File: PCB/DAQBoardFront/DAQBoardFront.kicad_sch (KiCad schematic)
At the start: 20 parts, among them J1 STM32F103C_Blue_Pill, J2 53375-0410, U1 Accelerometer, U2 AdafruitCANPal

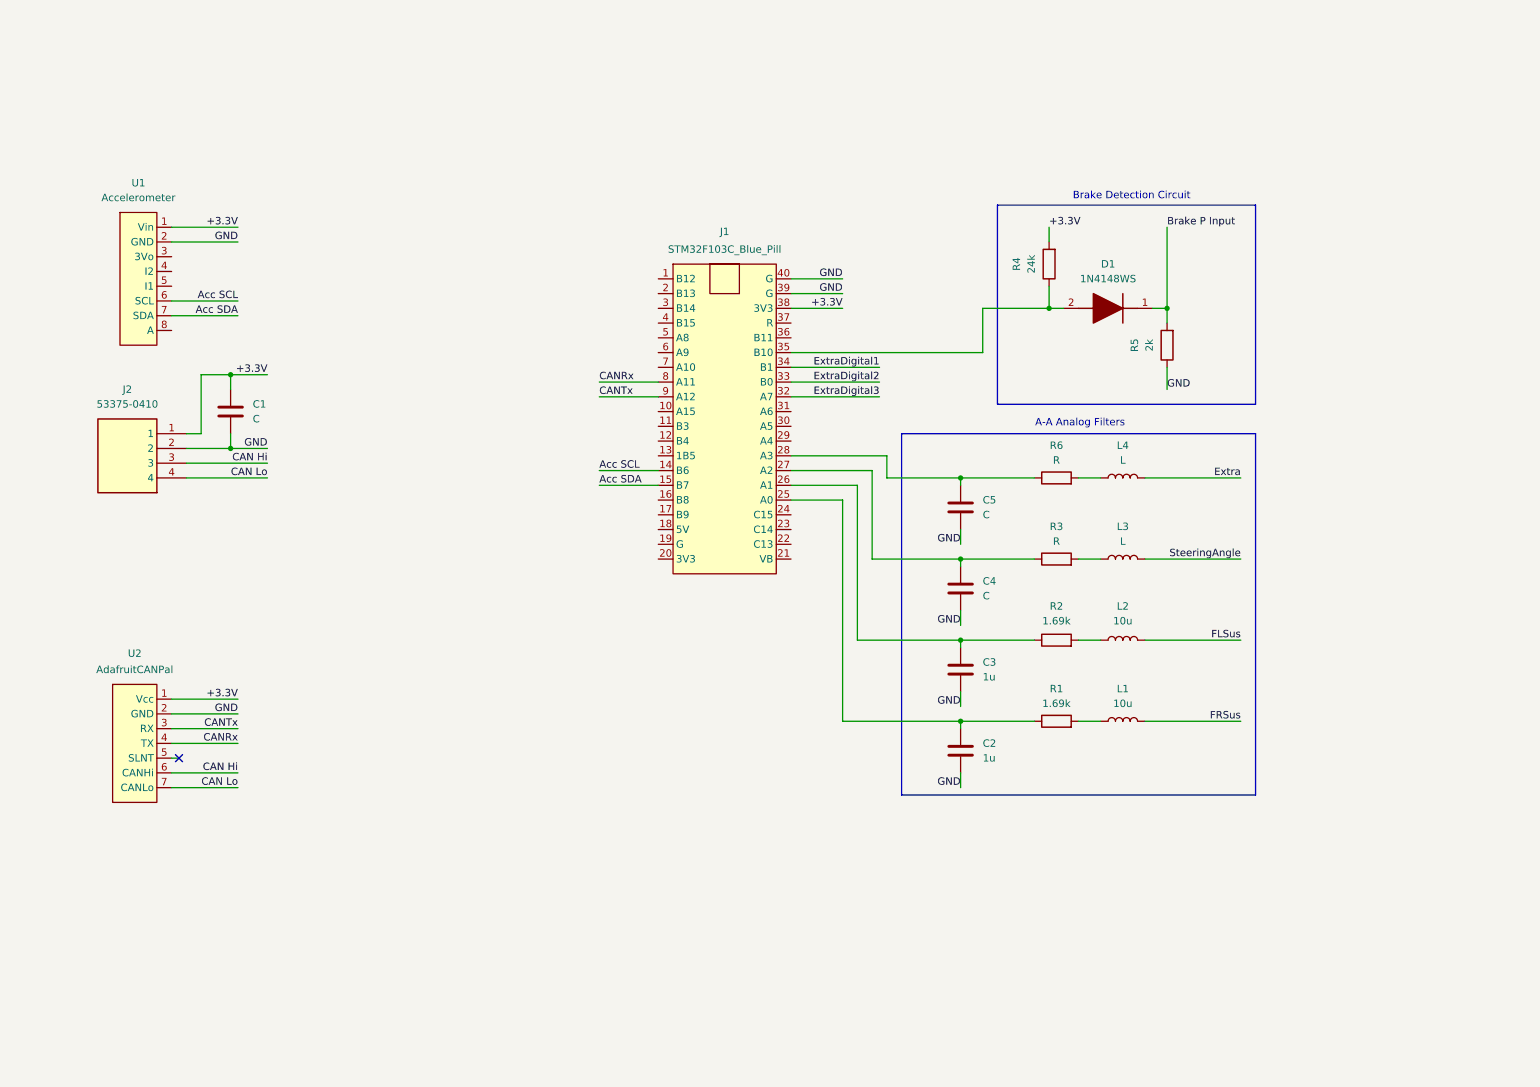
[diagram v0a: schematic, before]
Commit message: Initialized CFR symbol and footprint libraries, added git ignore file
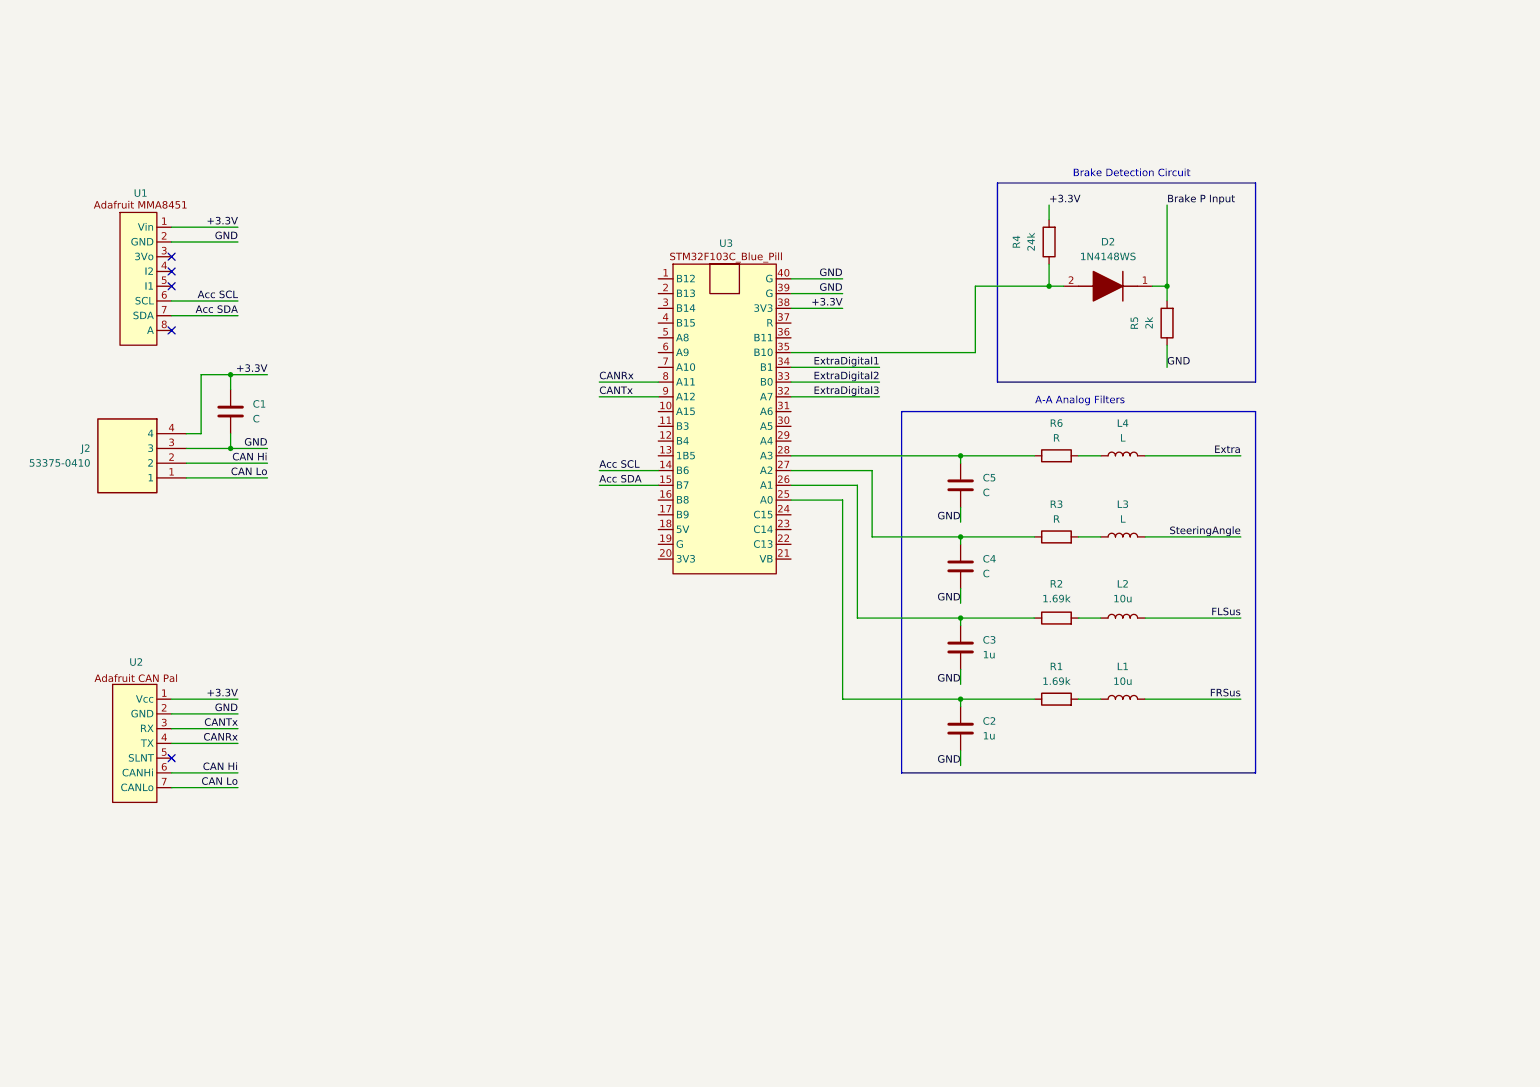
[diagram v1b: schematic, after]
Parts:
- removed D1: 1N4148WS, SODFL2512X90N, symbol 1N4148WS:1N4148WS
- removed J1: STM32F103C_Blue_Pill, symbol DAQ2027Lib:_Blue_Pill
- removed J2: 53375-0410, 0533750410, symbol 53375-0410:53375-0410
- removed U1: Accelerometer, symbol DAQ2027Lib:Adafruit_MMA8451
- removed U2: AdafruitCANPal, symbol DAQ2027Lib:Adafruit_CAN_Pal
- added D2: 1N4148WS, SODFL2512X90N, symbol CFR-Symbol-Library:1N4148WS
- added J2: 53375-0410, 0533750410, symbol CFR-Symbol-Library:53375-0410
- added U1: (no value), symbol CFR-Symbol-Library:Adafruit-MMA8451
- added U2: (no value), CFR-Footprint-Library:Adafruit CAN Pal, symbol CFR-Symbol-Library:Adafruit-CAN-Pal
- added U3: (no value), CFR-Footprint-Library:Blue-Pill, symbol CFR-Symbol-Library:Blue-Pill
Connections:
- net +3.3V: now also J2.4, U1.1 (Vin), U2.1 (Vcc), U3.38 (3V3)
- net Acc SCL: now also U1.6 (SCL), U3.14 (B6)
- net Acc SDA: now also U1.7 (SDA), U3.15 (B7)
- net Brake P Input: now also D2.1 (K)
- net CAN Hi: now also J2.2, U2.6 (CANHi)
- net CAN Lo: now also J2.1, U2.7 (CANLo)
- net CANRx: now also U2.4 (TX), U3.8 (A11)
- net CANTx: now also U2.3 (RX), U3.9 (A12)
- net ExtraDigital1: now also U3.34 (B1)
- net ExtraDigital2: now also U3.33 (B0)
- net ExtraDigital3: now also U3.32 (A7)
- net GND: now also J2.3, U1.2 (GND), U2.2 (GND), U3.39 (G), U3.40 (G)
- net at C2.1, R1.1: now also U3.25 (A0)
- net at C3.1, R2.1: now also U3.26 (A1)
- net at C4.1, R3.1: now also U3.27 (A2)
- net at C5.1, R6.1: now also U3.28 (A3)
- net at R4.1: now also D2.2 (A), U3.35 (B10)
- no-connect marks 1 -> 5
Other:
- moved on the sheet: C2, C3, C4, C5, L1, L2, L3, L4, R1, R2, R3, R4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

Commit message: Added more footprints/symbols for 8-pin input and SMD components
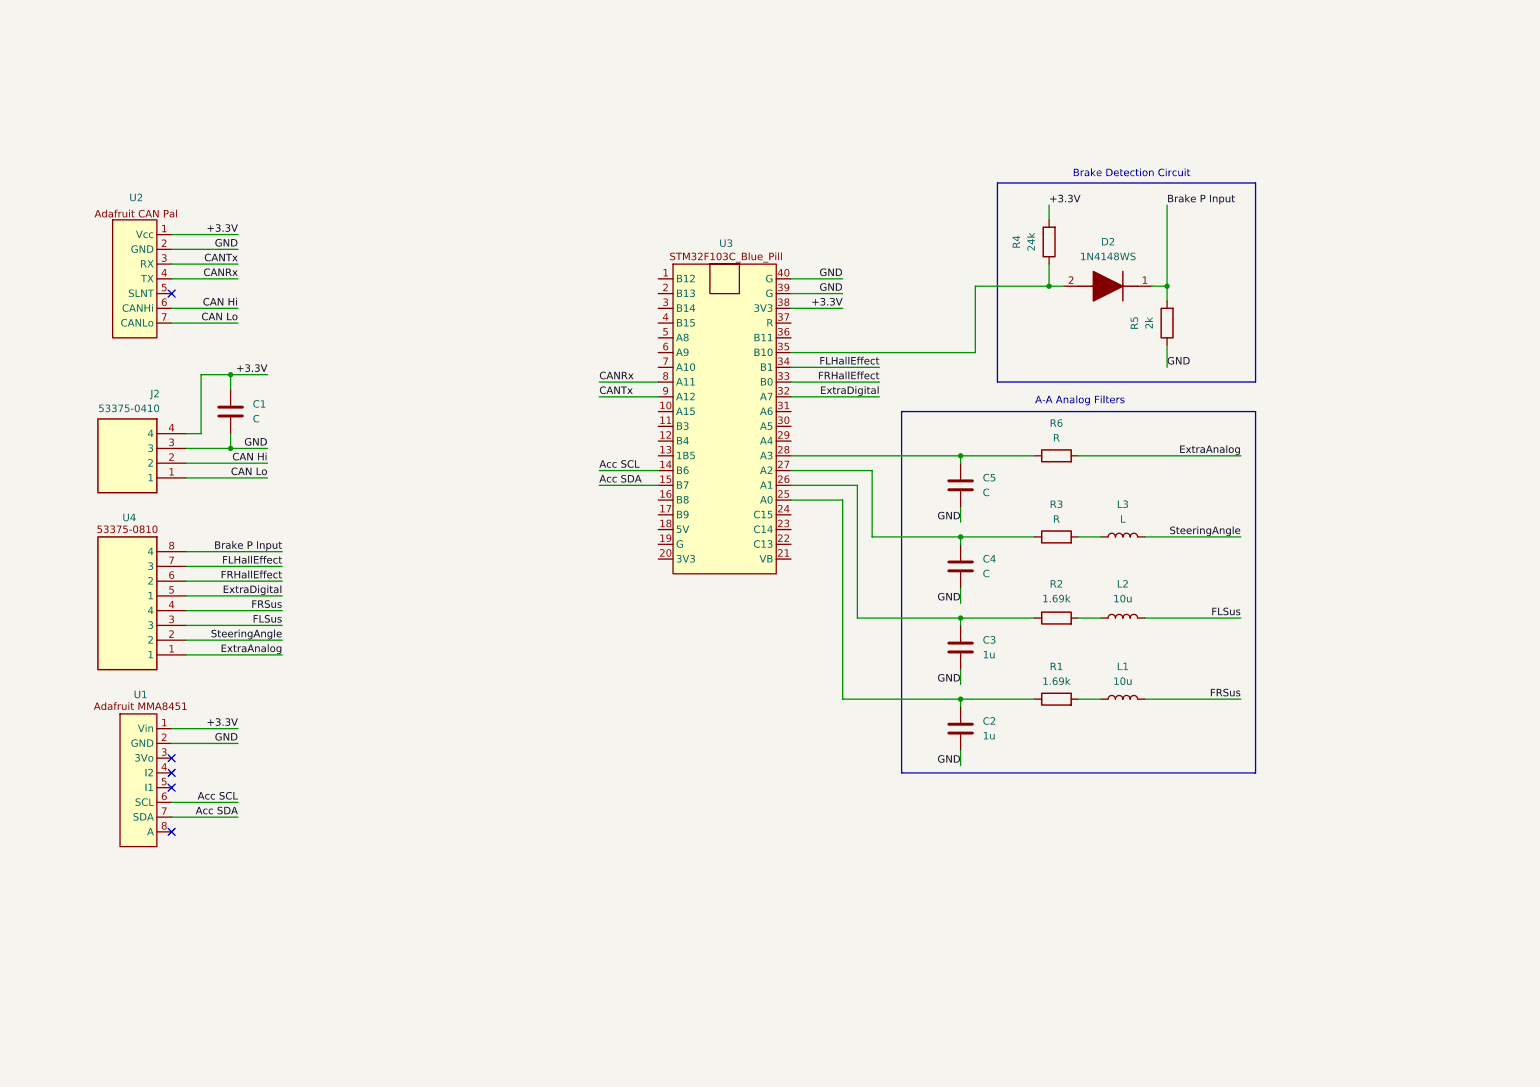
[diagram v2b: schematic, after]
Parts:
- removed L4: L, symbol Device:L
- added U4: (no value), CFR-Footprint-Library:CONN08_533750810_MOL, symbol CFR-Symbol-Library:53375-0810
- C1, C2, C3, C4, C5: footprint (none) -> Capacitor_SMD:C_0603_1608Metric_Pad1.08x0.95mm_HandSolder
- R1, R2, R3, R5, R6: footprint (none) -> Resistor_SMD:R_0603_1608Metric_Pad0.98x0.95mm_HandSolder
- R4: footprint (none) -> LED_SMD:LED_0603_1608Metric_Pad1.05x0.95mm_HandSolder
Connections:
- net Brake P Input: now also U4.8 (4)
- net FLSus: now also U4.3
- net FRSus: now also U4.4
- net SteeringAngle: now also U4.2
- net ExtraAnalog: now reaches R6.2
- net ExtraAnalog: now also U4.1
- net ExtraDigital1 renamed FLHallEffect
- net FLHallEffect: now also U4.7 (3)
- net ExtraDigital2 renamed FRHallEffect
- net FRHallEffect: now also U4.6 (2)
- net ExtraDigital3 renamed ExtraDigital
- net ExtraDigital: now also U4.5 (1)
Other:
- moved on the sheet: U1, U2

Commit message: Version 1.0 completed
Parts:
- L1, L2, L3: footprint (none) -> Inductor_SMD:L_0805_2012Metric_Pad1.05x1.20mm_HandSolder
- U1: footprint (none) -> CFR-Footprint-Library:MODULE_2019
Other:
- moved on the sheet: C1, C2, C3, C4, C5, D2, J2, L1, L2, L3, R1, R2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

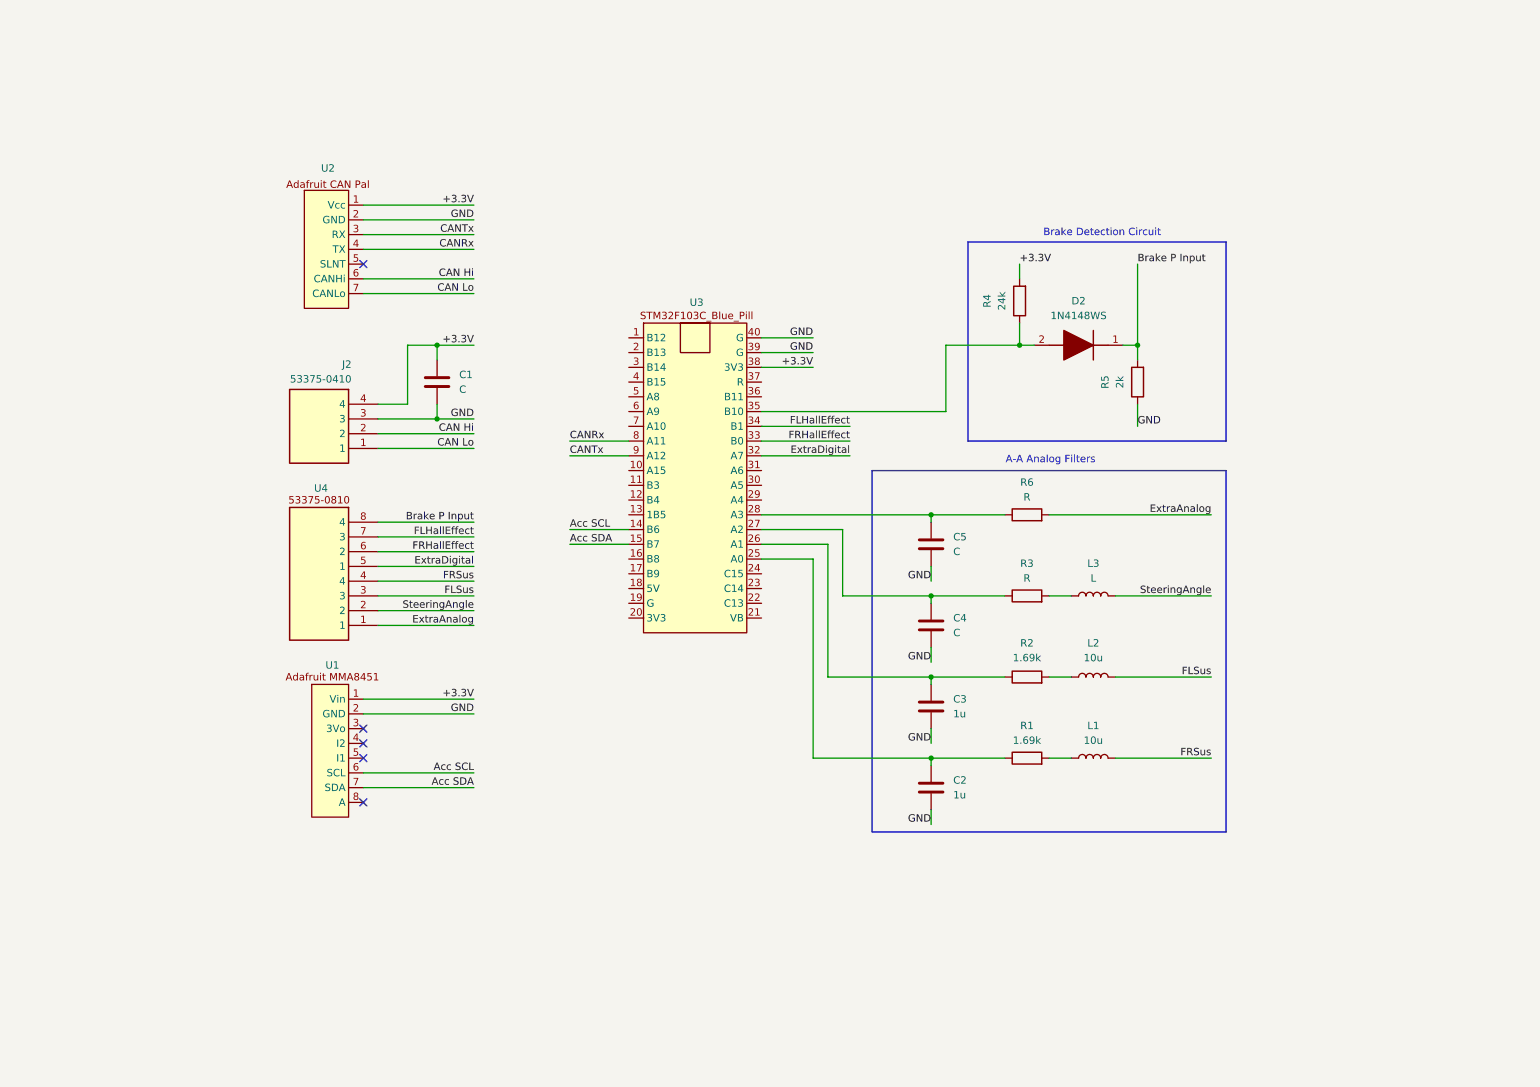
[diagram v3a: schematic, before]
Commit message: DAQ board moving towards multi-voltage level architecture & custom CAN module, WIP
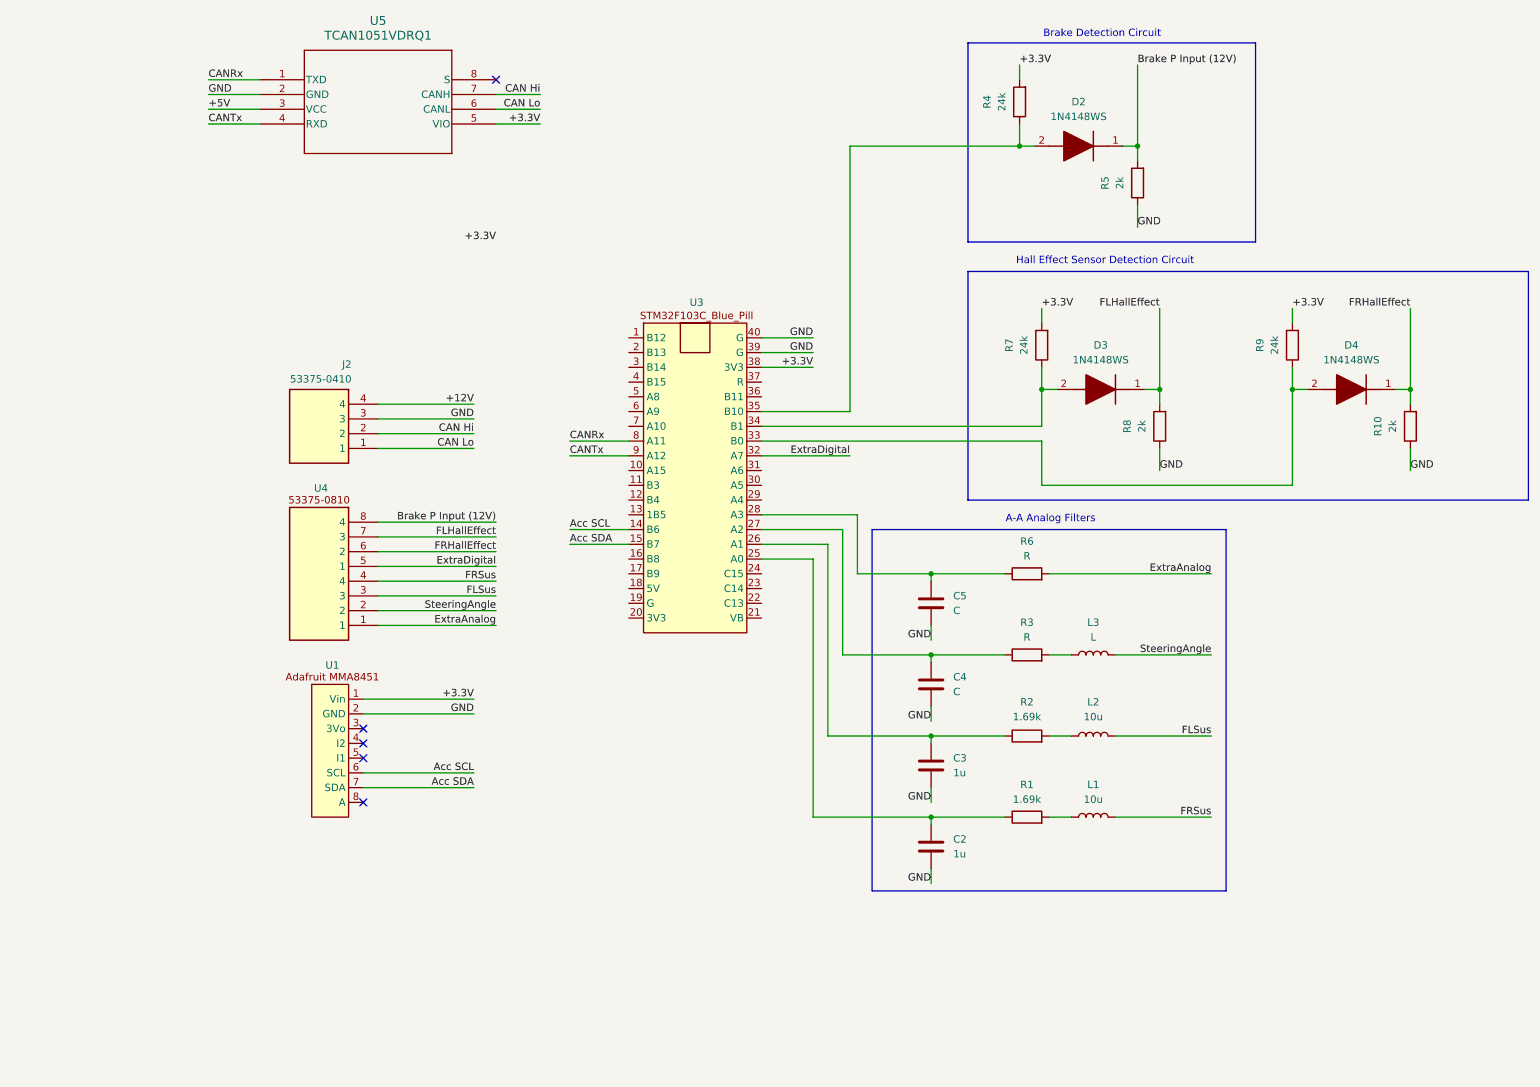
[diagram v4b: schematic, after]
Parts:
- removed C1: C, Capacitor_SMD:C_0603_1608Metric_Pad1.08x0.95mm_HandSolder, symbol Device:C
- removed U2: (no value), CFR-Footprint-Library:Adafruit CAN Pal, symbol CFR-Symbol-Library:Adafruit-CAN-Pal
- added D3, D4: 1N4148WS, SODFL2512X90N, symbol CFR-Symbol-Library:1N4148WS
- added R10, R8: 2k, Resistor_SMD:R_0603_1608Metric_Pad0.98x0.95mm_HandSolder, symbol Device:R
- added R7, R9: 24k, LED_SMD:LED_0603_1608Metric_Pad1.05x0.95mm_HandSolder, symbol Device:R
- added U5: TCAN1051VDRQ1, D8_TEX, symbol CFR-Symbol-Library:TCAN1051VDRQ1
- R4, R5: Rating (none) -> 1/4W
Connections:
- net +3.3V: now also R7.2, R9.2, U5.5 (VIO); no longer J2.4
- net CAN Hi: now also U5.7 (CANH)
- net CAN Lo: now also U5.6 (CANL)
- net CANRx: now also U5.1 (TXD)
- net CANTx: now also U5.4 (RXD)
- net FLHallEffect: now also D3.1 (K), R8.2; no longer U3.34 (B1)
- net FRHallEffect: now also D4.1 (K), R10.2; no longer U3.33 (B0)
- net GND: now also R10.1, R8.1, U5.2 (GND)
- net Brake P Input renamed Brake P Input (12V)
- new net: D4.2 (A), R9.1, U3.33 (B0)
- new net: D3.2 (A), R7.1, U3.34 (B1)
- new net +12V: J2.4
- new net +5V: U5.3 (VCC)
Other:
- note added: "Hall Effect Sensor Detection Circuit"
- moved on the sheet: C2, C3, C4, C5, D2, L1, L2, L3, R1, R2, R3, R4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
